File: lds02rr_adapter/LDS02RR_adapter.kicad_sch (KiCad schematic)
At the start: 4 parts, among them J2 JST PH F 4P VERT, Q1 AS2302

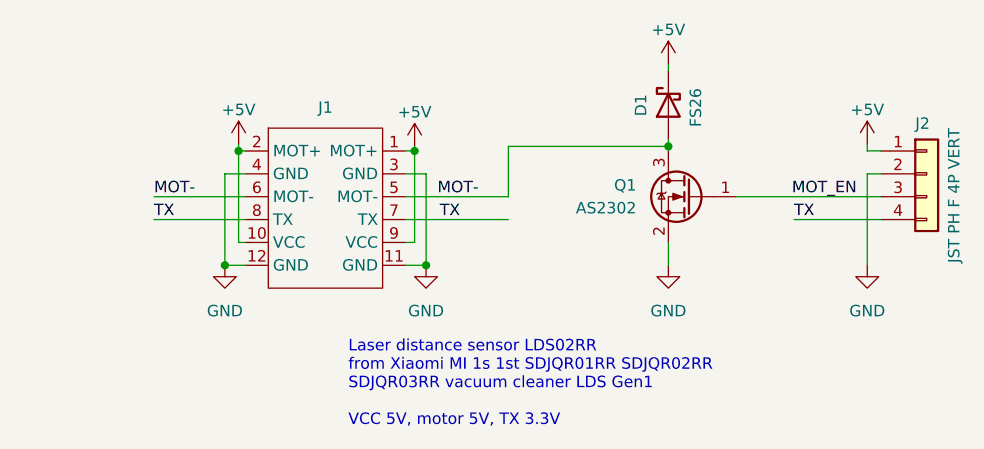
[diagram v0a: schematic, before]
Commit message: Neato, LDS02RR v0.2.0
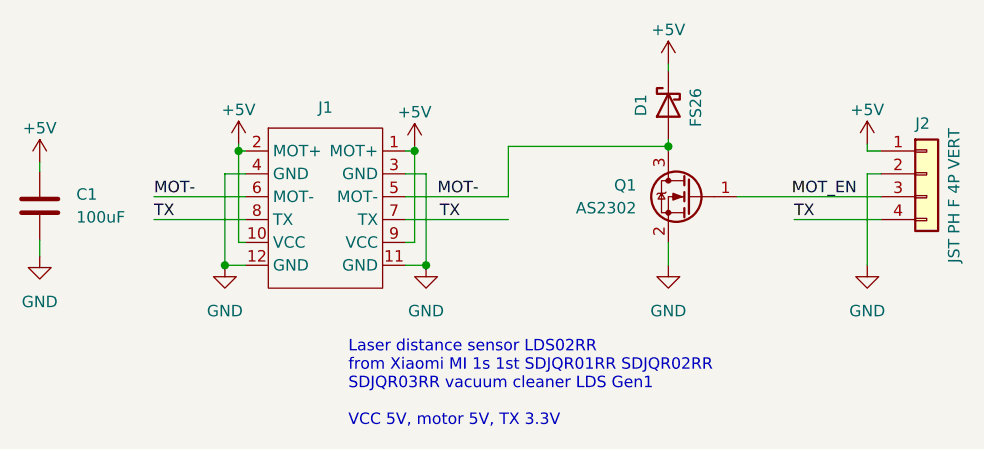
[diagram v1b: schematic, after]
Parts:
- added C1: 100uF, Capacitor_SMD:C_1206_3216Metric, symbol Device:C
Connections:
- net +5V: now also C1.1
- net GND: now also C1.2
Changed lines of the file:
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@@
   (title_block
     (title "LDS02RR adapter")
-    (date "2023-12-20")
-    (rev "0.1.0")
+    (date "2024-01-30")
+    (rev "0.2.0")
     (company "makerspet.com")
   )
@@
     (stroke (width 0) (type default))
   )
+  (wire (pts (xy 54.864 64.77) (xy 65.024 64.77))
+    (stroke (width 0) (type default))
+  )
+  (wire (pts (xy 82.804 59.69) (xy 85.09 59.69))
+    (stroke (width 0) (type default))
+  )
+  (wire (pts (xy 112.014 56.642) (xy 112.014 57.15))
+    (stroke (width 0) (type default))
+  )
+  (wire (pts (xy 64.262 57.15) (xy 65.024 57.15))
+    (stroke (width 0) (type default))
+  )
+  (wire (pts (xy 112.014 55.88) (xy 112.014 56.642))
+    (stroke (width 0) (type default))
+  )
+  (wire (pts (xy 112.014 56.642) (xy 94.234 56.642))
+    (stroke (width 0) (type default))
+  )
+  (wire (pts (xy 62.738 69.85) (xy 65.024 69.85))
+    (stroke (width 0) (type default))
+  )
+  (wire (pts (xy 112.014 67.31) (xy 112.014 69.85))
+    (stroke (width 0) (type default))
+  )
+  (wire (pts (xy 64.262 56.388) (xy 64.262 57.15))
+    (stroke (width 0) (type default))
+  )
+  (wire (pts (xy 82.804 62.23) (xy 94.234 62.23))
+    (stroke (width 0) (type default))
+  )
+  (wire (pts (xy 135.636 59.69) (xy 134.112 59.69))
+    (stroke (width 0) (type default))
+  )
+  (wire (pts (xy 83.82 57.15) (xy 82.804 57.15))
+    (stroke (width 0) (type default))
+  )
+  (wire (pts (xy 134.112 57.15) (xy 134.112 56.388))
+    (stroke (width 0) (type default))
+  )
+  (wire (pts (xy 83.82 56.642) (xy 83.82 57.15))
+    (stroke (width 0) (type default))
+  )
+  (wire (pts (xy 62.738 59.69) (xy 65.024 59.69))
+    (stroke (width 0) (type default))
+  )
+  (wire (pts (xy 119.634 62.23) (xy 135.636 62.23))
+    (stroke (width 0) (type default))
+  )
+  (wire (pts (xy 42.164 68.834) (xy 42.164 67.056))
+    (stroke (width 0) (type default))
+  )
+  (wire (pts (xy 94.234 56.642) (xy 94.234 62.23))
+    (stroke (width 0) (type default))
+  )
+  (wire (pts (xy 64.262 57.15) (xy 64.262 67.31))
+    (stroke (width 0) (type default))
+  )
+  (wire (pts (xy 83.82 57.15) (xy 83.82 67.31))
+    (stroke (width 0) (type default))
+  )
+  (wire (pts (xy 82.804 67.31) (xy 83.82 67.31))
+    (stroke (width 0) (type default))
+  )
+  (wire (pts (xy 125.984 64.77) (xy 135.636 64.77))
+    (stroke (width 0) (type default))
+  )
+  (wire (pts (xy 42.164 58.42) (xy 42.164 59.436))
+    (stroke (width 0) (type default))
+  )
+  (wire (pts (xy 85.09 69.85) (xy 85.09 59.69))
+    (stroke (width 0) (type default))
+  )
+  (wire (pts (xy 112.014 47.498) (xy 112.014 48.26))
+    (stroke (width 0) (type default))
+  )
   (wire (pts (xy 134.112 59.69) (xy 134.112 69.85))
-    (stroke (width 0) (type default))
-  )
-  (wire (pts (xy 54.864 64.77) (xy 65.024 64.77))
-    (stroke (width 0) (type default))
-  )
-  (wire (pts (xy 82.804 59.69) (xy 85.09 59.69))
-    (stroke (width 0) (type default))
-  )
-  (wire (pts (xy 112.014 56.642) (xy 112.014 57.15))
-    (stroke (width 0) (type default))
-  )
-  (wire (pts (xy 64.262 57.15) (xy 65.024 57.15))
-    (stroke (width 0) (type default))
-  )
-  (wire (pts (xy 112.014 55.88) (xy 112.014 56.642))
-    (stroke (width 0) (type default))
-  )
-  (wire (pts (xy 112.014 56.642) (xy 94.234 56.642))
-    (stroke (width 0) (type default))
-  )
-  (wire (pts (xy 62.738 69.85) (xy 65.024 69.85))
-    (stroke (width 0) (type default))
-  )
-  (wire (pts (xy 112.014 67.31) (xy 112.014 69.85))
-    (stroke (width 0) (type default))
-  )
-  (wire (pts (xy 64.262 56.388) (xy 64.262 57.15))
-    (stroke (width 0) (type default))
-  )
-  (wire (pts (xy 82.804 62.23) (xy 94.234 62.23))
-    (stroke (width 0) (type default))
-  )
-  (wire (pts (xy 135.636 59.69) (xy 134.112 59.69))
-    (stroke (width 0) (type default))
-  )
-  (wire (pts (xy 83.82 57.15) (xy 82.804 57.15))
-    (stroke (width 0) (type default))
-  )
-  (wire (pts (xy 134.112 57.15) (xy 134.112 56.388))
-    (stroke (width 0) (type default))
-  )
-  (wire (pts (xy 83.82 56.642) (xy 83.82 57.15))
-    (stroke (width 0) (type default))
-  )
-  (wire (pts (xy 62.738 59.69) (xy 65.024 59.69))
-    (stroke (width 0) (type default))
-  )
-  (wire (pts (xy 119.634 62.23) (xy 135.636 62.23))
-    (stroke (width 0) (type default))
-  )
-  (wire (pts (xy 94.234 56.642) (xy 94.234 62.23))
-    (stroke (width 0) (type default))
-  )
-  (wire (pts (xy 64.262 57.15) (xy 64.262 67.31))
-    (stroke (width 0) (type default))
-  )
-  (wire (pts (xy 83.82 57.15) (xy 83.82 67.31))
-    (stroke (width 0) (type default))
-  )
-  (wire (pts (xy 82.804 67.31) (xy 83.82 67.31))
-    (stroke (width 0) (type default))
-  )
-  (wire (pts (xy 125.984 64.77) (xy 135.636 64.77))
-    (stroke (width 0) (type default))
-  )
-  (wire (pts (xy 85.09 69.85) (xy 85.09 59.69))
-    (stroke (width 0) (type default))
-  )
-  (wire (pts (xy 112.014 47.498) (xy 112.014 48.26))
     (stroke (width 0) (type default))
   )
@@
     )
   )
+  (symbol (lib_id "power:+5V") (at 42.164 58.42 0) (unit 1)
+    (in_bom yes) (on_board yes) (dnp no) (fields_autoplaced)
+    (property "Reference" "#PWR09" (at 42.164 62.23 0)
+      (effects (font (size 1.27 1.27)) hide)
+    )
+    (property "Value" "+5V" (at 42.164 54.61 0)
+      (effects (font (size 1.27 1.27)))
+    )
+    (property "Footprint" "" (at 42.164 58.42 0)
+      (effects (font (size 1.27 1.27)) hide)
+    )
+    (property "Datasheet" "" (at 42.164 58.42 0)
+      (effects (font (size 1.27 1.27)) hide)
+    )
+    (pin "1")
+    (instances
+      (project "LDS02RR_adapter"
+        (path "/c13da21a-388e-44a0-831a-aa3d56cf7c53"
+          (reference "#PWR09") (unit 1)
+        )
+      )
+      (project "esp32_breakout"
+        (path "/e24ae185-8f18-408c-aee8-f727519bade3"
+          (reference "#PWR012") (unit 1)
+        )
+      )
+    )
+  )
+  (symbol (lib_id "Device:C") (at 42.164 63.246 0) (unit 1)
+    (in_bom yes) (on_board yes) (dnp no) (fields_autoplaced)
+    (property "Reference" "C1" (at 46.228 61.976 0)
+      (effects (font (size 1.27 1.27)) (justify left))
+    )
+    (property "Value" "100uF" (at 46.228 64.516 0)
+      (effects (font (size 1.27 1.27)) (justify left))
+    )
+    (property "Footprint" "Capacitor_SMD:C_1206_3216Metric" (at 43.1292 67.056 0)
+      (effects (font (size 1.27 1.27)) hide)
+    )
+    (property "Datasheet" "~" (at 42.164 63.246 0)
+      (effects (font (size 1.27 1.27)) hide)
+    )
+    (pin "1")
+    (pin "2")
+    (instances
+      (project "LDS02RR_adapter"
+        (path "/c13da21a-388e-44a0-831a-aa3d56cf7c53"
+          (reference "C1") (unit 1)
+        )
+      )
+    )
+  )
   (symbol (lib_id "power:+5V") (at 64.262 56.388 0) (unit 1)
     (in_bom yes) (on_board yes) (dnp no) (fields_autoplaced)
@@
         )
       )
+    )
+  )
+  (symbol (lib_id "power:GND") (at 42.164 68.834 0) (unit 1)
+    (in_bom yes) (on_board yes) (dnp no) (fields_autoplaced)
+    (property "Reference" "#PWR010" (at 42.164 75.184 0)
+      (effects (font (size 1.27 1.27)) hide)
+    )
+    (property "Value" "GND" (at 42.164 73.914 0)
+      (effects (font (size 1.27 1.27)))
+    )
+    (property "Footprint" "" (at 42.164 68.834 0)
+      (effects (font (size 1.27 1.27)) hide)
+    )
+    (property "Datasheet" "" (at 42.164 68.834 0)
+      (effects (font (size 1.27 1.27)) hide)
+    )
+    (pin "1")
+    (instances
+      (project "LDS02RR_adapter"
+        (path "/c13da21a-388e-44a0-831a-aa3d56cf7c53"
+          (reference "#PWR010") (unit 1)
+        )
+      )
+      (project "esp32_breakout"
+        (path "/e24ae185-8f18-408c-aee8-f727519bade3"
+          (reference "#PWR011") (unit 1)
+        )
+      )

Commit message: 0603 bypass cap
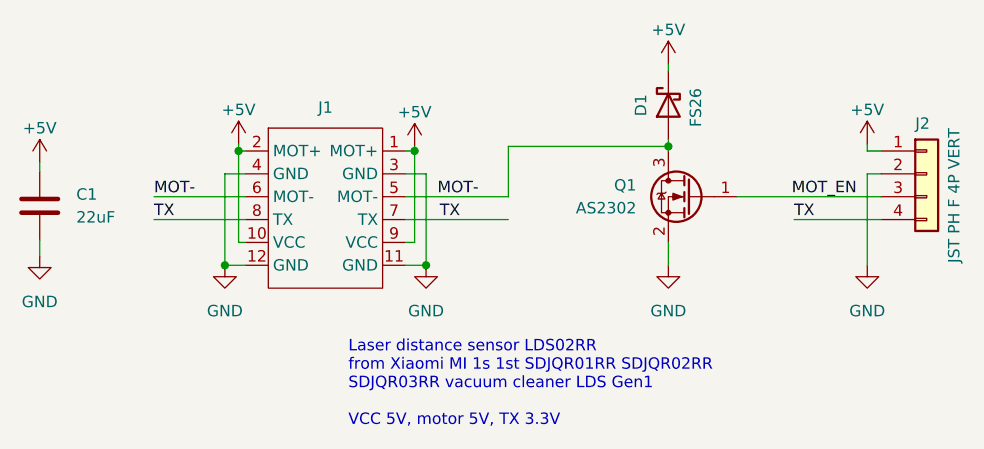
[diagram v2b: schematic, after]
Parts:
- C1: value 100uF -> 22uF; footprint Capacitor_SMD:C_1206_3216Metric -> Capacitor_SMD:C_0603_1608Metric
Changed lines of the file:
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@@
   (title_block
     (title "LDS02RR adapter")
-    (date "2024-01-30")
-    (rev "0.2.0")
+    (date "2024-03-06")
+    (rev "0.2.1")
     (company "makerspet.com")
   )
@@
       (effects (font (size 1.27 1.27)) (justify left))
     )
-    (property "Value" "100uF" (at 46.228 64.516 0)
+    (property "Value" "22uF" (at 46.228 64.516 0)
       (effects (font (size 1.27 1.27)) (justify left))
     )
-    (property "Footprint" "Capacitor_SMD:C_1206_3216Metric" (at 43.1292 67.056 0)
-      (effects (font (size 1.27 1.27)) hide)
-    )
+    (property "Footprint" "Capacitor_SMD:C_0603_1608Metric" (at 43.1292 67.056 0)
+      (effects (font (size 1.27 1.27)) hide)
+    )
